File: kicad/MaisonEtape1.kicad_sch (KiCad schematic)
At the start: 45 parts, among them J13 Conn_01x08_Socket, J14 Conn_01x08_Socket, J4 AVR-ISP-6, U1 ATmega8A-A, U1_XT1 Conn_01x09, U2 ATmega8A-A, U2_XT1 Conn_01x09, U9 DS1621, Y3 Crystal

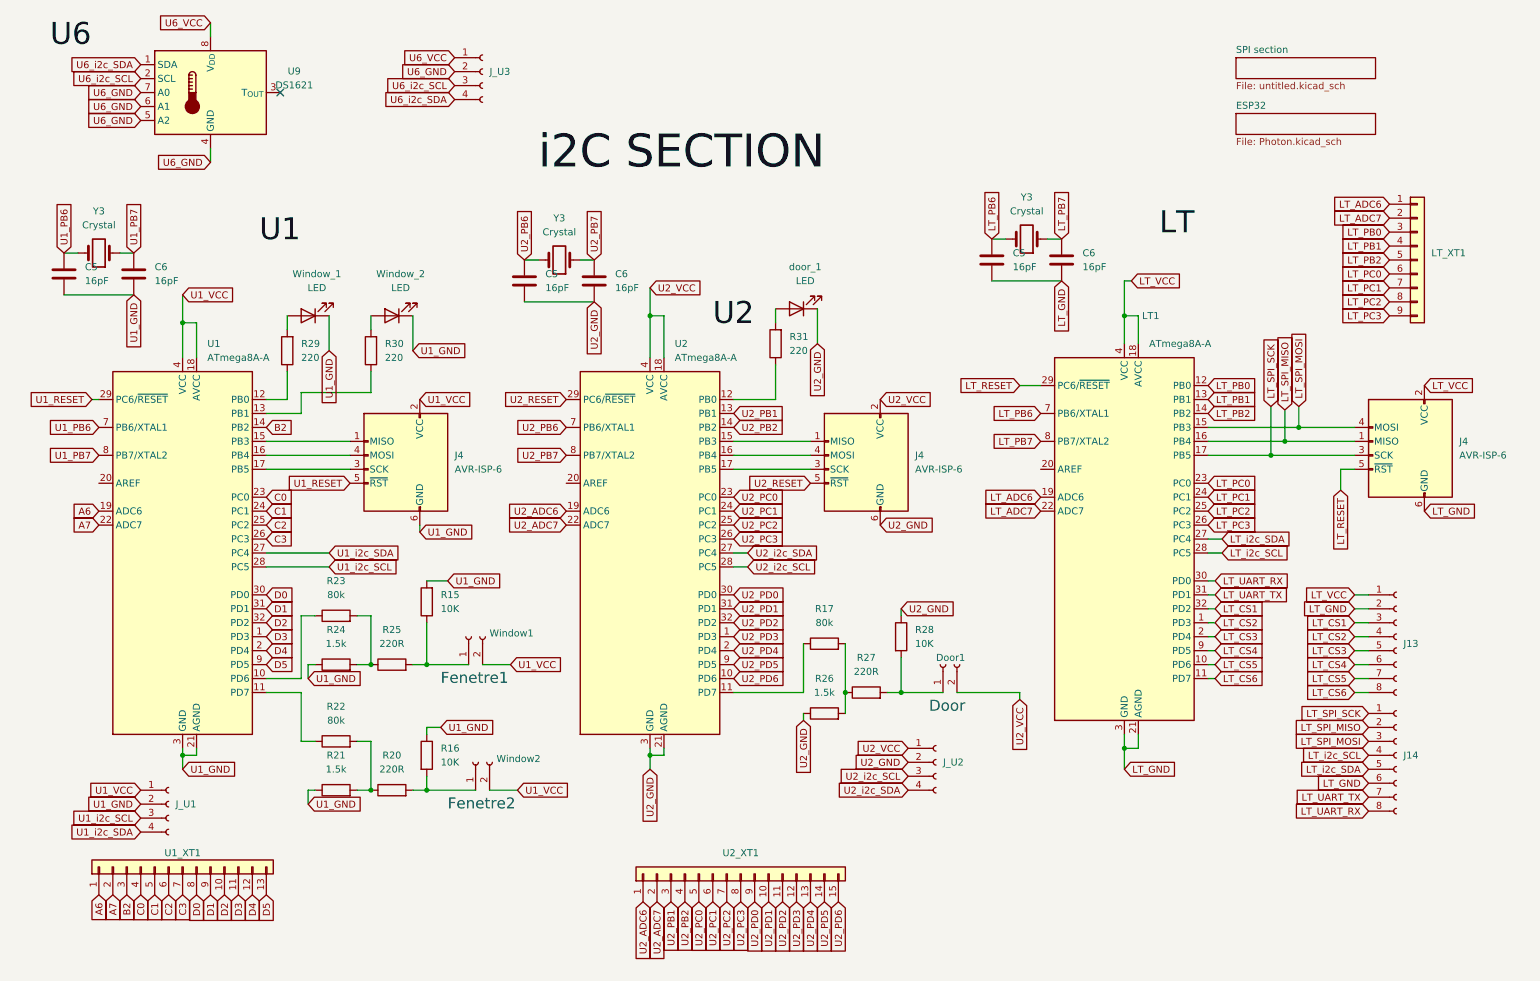
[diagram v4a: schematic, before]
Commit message: switch to SPIs
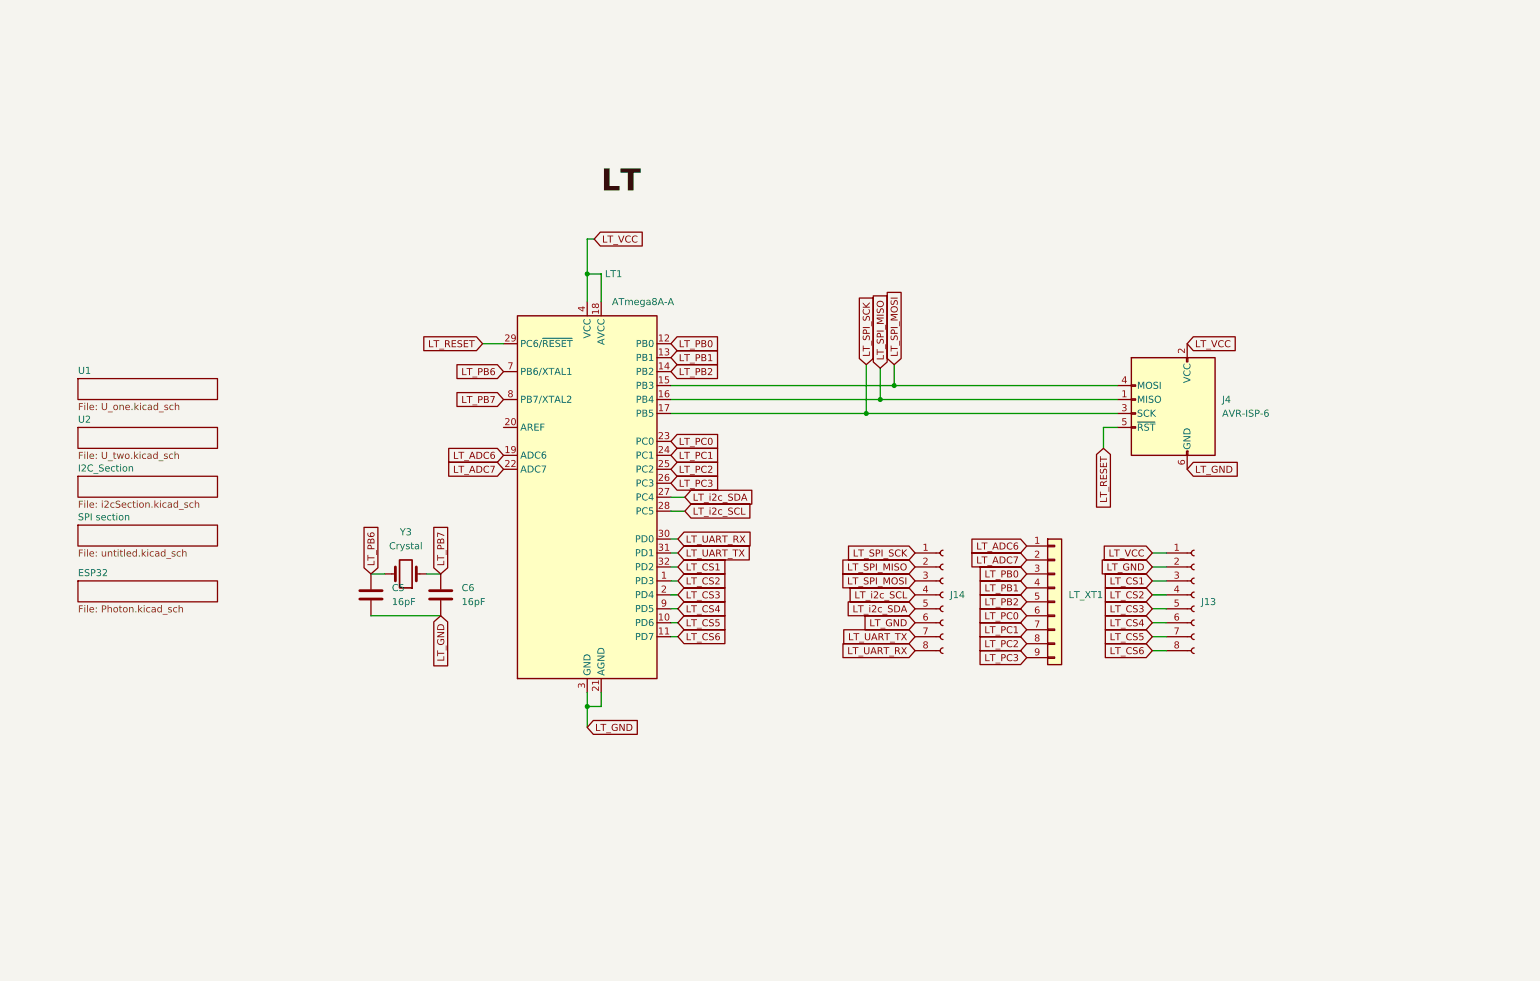
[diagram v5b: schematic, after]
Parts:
- removed C5 (x2), C6 (x2): 16pF, Capacitor_SMD:C_0805_2012Metric_Pad1.18x1.45mm_HandSolder, symbol Device:C
- removed Door1, Window1, Window2: Conn_01x02_Socket, Connector_PinSocket_2.54mm:PinSocket_1x02_P2.54mm_Vertical, symbol Connector:Conn_01x02_Socket
- removed J4 (x2): AVR-ISP-6, JPLibrary:SPI_prog, symbol Connector:AVR-ISP-6
- removed J_U1, J_U2, J_U3: Conn_01x04_Socket, Connector_PinHeader_2.54mm:PinHeader_1x04_P2.54mm_Vertical, symbol Connector:Conn_01x04_Socket
- removed R15, R16, R28: 10K, Resistor_SMD:R_0805_2012Metric_Pad1.20x1.40mm_HandSolder, symbol Device:R
- removed R17, R22, R23: 80k, Resistor_SMD:R_0805_2012Metric_Pad1.20x1.40mm_HandSolder, symbol Device:R
- removed R20, R25, R27: 220R, Resistor_SMD:R_0805_2012Metric_Pad1.20x1.40mm_HandSolder, symbol Device:R
- removed R21, R24, R26: 1.5k, Resistor_SMD:R_0805_2012Metric_Pad1.20x1.40mm_HandSolder, symbol Device:R
- removed R29, R30, R31: 220, Resistor_SMD:R_0805_2012Metric_Pad1.20x1.40mm_HandSolder, symbol Device:R
- removed U1, U2: ATmega8A-A, Package_QFP:TQFP-32_7x7mm_P0.8mm, symbol MCU_Microchip_ATmega:ATmega8A-A
- removed U1_XT1: Conn_01x09, JP_Library:XT_13, symbol Connector_Generic:Conn_01x13
- removed U2_XT1: Conn_01x09, JP_Library:XT_15, symbol Connector_Generic:Conn_01x15
- removed U9: DS1621, Package_DIP:DIP-8_W7.62mm, symbol Sensor_Temperature:DS1621
- removed Window_1, Window_2, door_1: LED, LED_SMD:LED_0805_2012Metric, symbol Device:LED
- removed Y3 (x2): Crystal, JP_Library:Crystal 49SS-SMD, symbol Device:Crystal
- J4: footprint JPLibrary:SPI_prog -> JP_Library:SPI_prog
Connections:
- no-connect marks 1 -> 0
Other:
- added sheet I2C_Section (i2cSection.kicad_sch)
- added sheet U1 (U_one.kicad_sch)
- added sheet U2 (U_two.kicad_sch)
- note removed: "Door"
- note removed: "Fenetre1"
- note removed: "Fenetre2"
- moved on the sheet: C5, C6, J13, J14, J4, LT1, LT_XT1, Y3
